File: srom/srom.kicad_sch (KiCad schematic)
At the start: 18 parts, among them J1 Conn_01x03_Female, Q1 PMBT2222A, U1 4075, U4 74LS245, U5 Pico-1 ROM

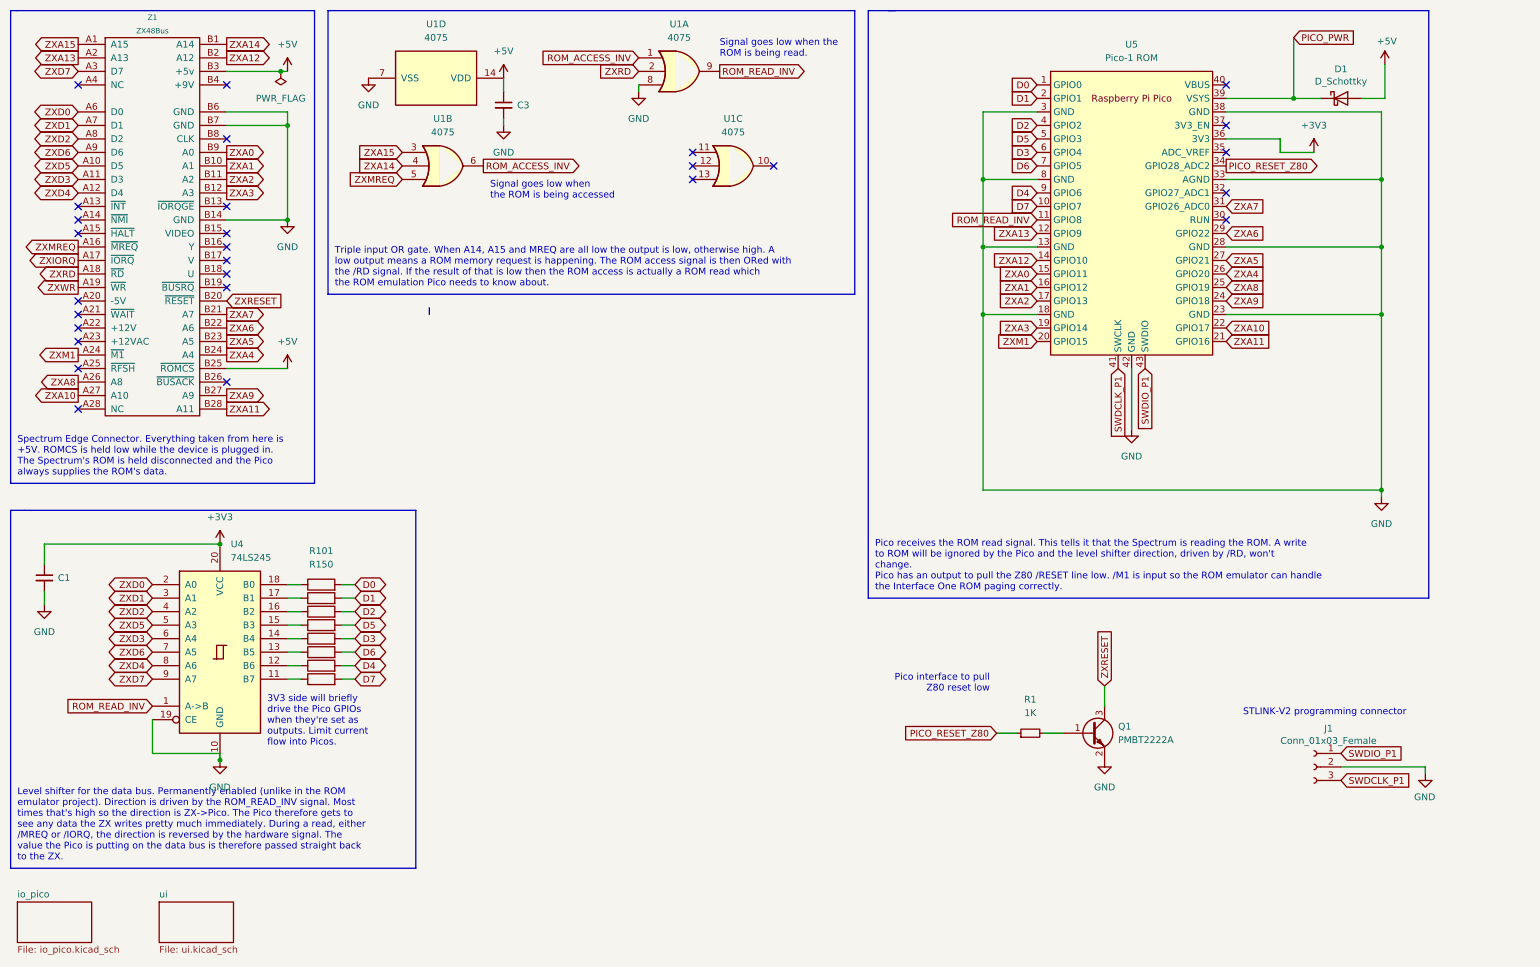
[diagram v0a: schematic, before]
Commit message: break out the 3V3 supplies into separate ones
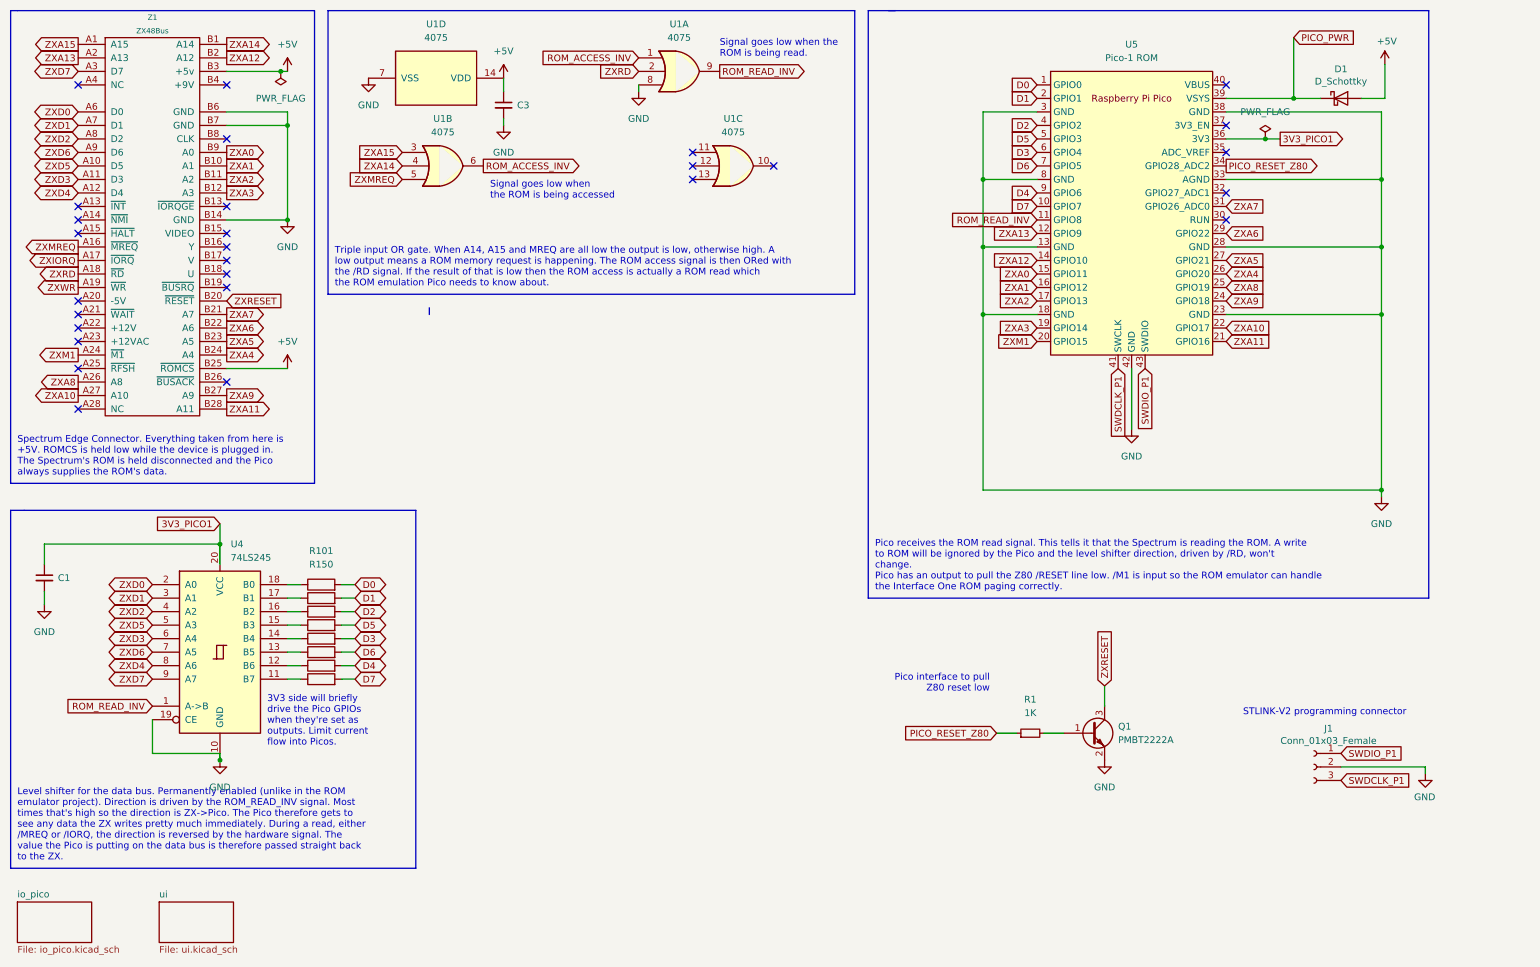
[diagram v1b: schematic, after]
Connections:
- net +3V3 renamed 3V3_PICO1
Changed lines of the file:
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@@
     (title "Pico Interface One")
     (date "2023-03-01")
-    (rev "v1.1")
+    (rev "v1.1 to v1.2 WIP")
+  )
+  (junction (at 196.85 72.39) (diameter 0) (color 0 0 0 0)
+  )
+  (junction (at 249.936 39.37) (diameter 0) (color 0 0 0 0)
   )
   (junction (at 53.34 115.57) (diameter 0) (color 0 0 0 0)
-  )
-  (junction (at 196.85 72.39) (diameter 0) (color 0 0 0 0)
   )
   (junction (at 196.85 59.69) (diameter 0) (color 0 0 0 0)
@@
     (stroke (width 0) (type default) (color 0 0 0 0))
   )
+  (wire (pts (xy 249.936 39.37) (xy 252.73 39.37))
+    (stroke (width 0) (type default) (color 0 0 0 0))
+  )
   (wire (pts (xy 54.61 26.67) (xy 64.77 26.67))
     (stroke (width 0) (type default) (color 0 0 0 0))
@@
     (stroke (width 0) (type default) (color 0 0 0 0))
   )
-  (wire (pts (xy 252.73 39.37) (xy 252.73 41.91))
-    (stroke (width 0) (type default) (color 0 0 0 0))
-  )
   (polyline (pts (xy 71.12 15.24) (xy 71.12 104.14))
     (stroke (width 0) (type default) (color 0 0 0 0))
@@
     (stroke (width 0) (type default) (color 0 0 0 0))
   )
+  (wire (pts (xy 53.34 115.57) (xy 53.34 119.38))
+    (stroke (width 0) (type default) (color 0 0 0 0))
+  )
   (wire (pts (xy 196.85 46.99) (xy 207.01 46.99))
     (stroke (width 0) (type default) (color 0 0 0 0))
@@
     (stroke (width 0) (type default) (color 0 0 0 0))
   )
-  (wire (pts (xy 252.73 41.91) (xy 259.08 41.91))
-    (stroke (width 0) (type default) (color 0 0 0 0))
-  )
   (wire (pts (xy 106.68 27.94) (xy 106.68 30.48))
     (stroke (width 0) (type default) (color 0 0 0 0))
@@
     (stroke (width 0) (type default) (color 0 0 0 0))
   )
+  (wire (pts (xy 53.34 111.76) (xy 53.34 115.57))
+    (stroke (width 0) (type default) (color 0 0 0 0))
+  )
   (wire (pts (xy 207.01 34.29) (xy 196.85 34.29))
     (stroke (width 0) (type default) (color 0 0 0 0))
@@
     (stroke (width 0) (type default) (color 0 0 0 0))
   )
-  (wire (pts (xy 242.57 39.37) (xy 252.73 39.37))
+  (wire (pts (xy 242.57 39.37) (xy 249.936 39.37))
     (stroke (width 0) (type default) (color 0 0 0 0))
   )
@@
     )
   )
+  (global_label "3V3_PICO1" (shape output) (at 252.73 39.37 0) (fields_autoplaced)
+    (effects (font (size 1.27 1.27)) (justify left))
+    (property "Intersheet References" "${INTERSHEET_REFS}" (id 0) (at 265.3031 39.2906 0)
+      (effects (font (size 1.27 1.27)) (justify left) hide)
+    )
+  )
   (global_label "D6" (shape input) (at 207.01 44.45 180) (fields_autoplaced)
     (effects (font (size 1.27 1.27)) (justify right))
@@
     )
   )
+  (global_label "3V3_PICO1" (shape input) (at 53.34 111.76 180) (fields_autoplaced)
+    (effects (font (size 1.27 1.27)) (justify right))
+    (property "Intersheet References" "${INTERSHEET_REFS}" (id 0) (at 40.7669 111.6806 0)
+      (effects (font (size 1.27 1.27)) (justify right) hide)
+    )
+  )
   (global_label "ZXA0" (shape input) (at 207.01 64.77 180) (fields_autoplaced)
     (effects (font (size 1.27 1.27)) (justify right))
@@
       (effects (font (size 1.27 1.27)) (justify right) hide)
     )
+  )
+  (symbol (lib_id "power:PWR_FLAG") (at 249.936 39.37 0) (unit 1)
+    (in_bom yes) (on_board yes) (fields_autoplaced)
+    (property "Reference" "#FLG0102" (id 0) (at 249.936 37.465 0)
+      (effects (font (size 1.27 1.27)) hide)
+    )
+    (property "Value" "PWR_FLAG" (id 1) (at 249.936 34.29 0))
+    (property "Footprint" "" (id 2) (at 249.936 39.37 0)
+      (effects (font (size 1.27 1.27)) hide)
+    )
+    (property "Datasheet" "~" (id 3) (at 249.936 39.37 0)
+      (effects (font (size 1.27 1.27)) hide)
+    )
+    (pin "1")
   )
   (symbol (lib_id "power:+5V") (at 272.415 25.4 0) (unit 1)
@@
     (pin "1")
     (pin "2")
-  )
-  (symbol (lib_id "power:+3V3") (at 259.08 41.91 0) (unit 1)
-    (in_bom yes) (on_board yes)
-    (property "Reference" "#PWR0101" (id 0) (at 259.08 45.72 0)
-      (effects (font (size 1.27 1.27)) hide)
-    )
-    (property "Value" "+3V3" (id 1) (at 259.08 36.83 0))
-    (property "Footprint" "" (id 2) (at 259.08 41.91 0)
-      (effects (font (size 1.27 1.27)) hide)
-    )
-    (property "Datasheet" "" (id 3) (at 259.08 41.91 0)
-      (effects (font (size 1.27 1.27)) hide)
-    )
-    (pin "1")
-  )
-  (symbol (lib_id "power:+3V3") (at 53.34 115.57 0) (unit 1)
-    (in_bom yes) (on_board yes) (fields_autoplaced)
-    (property "Reference" "#PWR010" (id 0) (at 53.34 119.38 0)
-      (effects (font (size 1.27 1.27)) hide)
-    )
-    (property "Value" "+3V3" (id 1) (at 53.34 110.49 0))
-    (property "Footprint" "" (id 2) (at 53.34 115.57 0)
-      (effects (font (size 1.27 1.27)) hide)
-    )
-    (property "Datasheet" "" (id 3) (at 53.34 115.57 0)
-      (effects (font (size 1.27 1.27)) hide)
-    )
-    (pin "1")
   )
   (symbol (lib_id "Device:R") (at 72.39 130.81 90) (unit 1)
@@
       (reference "#FLG0101") (unit 1) (value "PWR_FLAG") (footprint "")
     )
+    (path "/00435cad-35db-4d8c-a211-1a67f7361e91"
+      (reference "#FLG0102") (unit 1) (value "PWR_FLAG") (footprint "")
+    )
+    (path "/95a6eb69-d4c1-4a7e-a8e8-144430faf0e2/25fce74c-db7d-439d-b46a-e7ee4fba7d1a"
+      (reference "#FLG0103") (unit 1) (value "PWR_FLAG") (footprint "")
+    )
+    (path "/acda4c69-0a65-473b-ab4f-e765252d7da2/47f1e06f-c0f4-47be-b2ea-94c67d89ef70"
+      (reference "#FLG0104") (unit 1) (value "PWR_FLAG") (footprint "")
+    )
     (path "/acda4c69-0a65-473b-ab4f-e765252d7da2/334e052e-8ff6-4bbe-a873-da87ff53ae91"
       (reference "#FLG0301") (unit 1) (value "PWR_FLAG") (footprint "")
@@
       (reference "#PWR05") (unit 1) (value "+5V") (footprint "")
     )
-    (path "/680d1fc8-3a19-4cac-a3b2-5242d9ba4ad5"
-      (reference "#PWR010") (unit 1) (value "+3V3") (footprint "")
-    )
     (path "/e65b2d50-1512-4b2c-8e99-2f26673148c8"
       (reference "#PWR011") (unit 1) (value "GND") (footprint "")
@@
       (reference "#PWR016") (unit 1) (value "GND") (footprint "")
     )
-    (path "/64ca279f-08b9-4ba5-8585-3fc2b834e6f0"
-      (reference "#PWR0101") (unit 1) (value "+3V3") (footprint "")
-    )
     (path "/5344e888-6e86-4b4d-8c03-ed4967b31a8a"
       (reference "#PWR0102") (unit 1) (value "GND") (footprint "")
@@
       (reference "#PWR0201") (unit 1) (value "GND") (footprint "")
     )
-    (path "/95a6eb69-d4c1-4a7e-a8e8-144430faf0e2/c54c1e8a-e59e-4902-8ed1-8aca0d40aa2d"
-      (reference "#PWR0202") (unit 1) (value "+3V3") (footprint "")
-    )
     (path "/95a6eb69-d4c1-4a7e-a8e8-144430faf0e2/b4561307-559f-491e-95d1-1c57e89e9bd0"
       (reference "#PWR0203") (unit 1) (value "GND") (footprint "")
@@
       (reference "#PWR0204") (unit 1) (value "GND") (footprint "")
     )
-    (path "/95a6eb69-d4c1-4a7e-a8e8-144430faf0e2/31ee41c8-2e5c-4998-bf70-c3af77f7450a"
-      (reference "#PWR0205") (unit 1) (value "+3V3") (footprint "")
-    )
-    (path "/95a6eb69-d4c1-4a7e-a8e8-144430faf0e2/da16d1c0-e0fb-438f-b16b-b7064b2070b2"
-      (reference "#PWR0206") (unit 1) (value "+3V3") (footprint "")
-    )
     (path "/95a6eb69-d4c1-4a7e-a8e8-144430faf0e2/74d2792e-dc2e-4c26-bfe0-64794fa1d06e"
       (reference "#PWR0207") (unit 1) (value "GND") (footprint "")
@@
       (reference "#PWR0301") (unit 1) (value "GND") (footprint "")
     )
-    (path "/acda4c69-0a65-473b-ab4f-e765252d7da2/2f004ed8-568a-4db0-ae25-4b856d05e91a"
-      (reference "#PWR0302") (unit 1) (value "+3V3") (footprint "")
-    )
     (path "/acda4c69-0a65-473b-ab4f-e765252d7da2/9111f657-cc15-4eeb-9b4d-78f61ca6b08c"
       (reference "#PWR0303") (unit 1) (value "GND") (footprint "")
@@
       (reference "#PWR0304") (unit 1) (value "GND") (footprint "")
     )
-    (path "/acda4c69-0a65-473b-ab4f-e765252d7da2/0b79a16b-da0b-469f-b1f2-b6265ed1490c"
-      (reference "#PWR0305") (unit 1) (value "+3V3") (footprint "")
-    )
-    (path "/acda4c69-0a65-473b-ab4f-e765252d7da2/9fa9b51b-82ff-40db-902e-69e5796d2d81"
-      (reference "#PWR0306") (unit 1) (value "+3V3") (footprint "")
-    )
     (path "/acda4c69-0a65-473b-ab4f-e765252d7da2/a58c7f3b-6519-4b5a-8453-2d4882e5998e"
       (reference "#PWR0307") (unit 1) (value "GND") (footprint "")
@@
       (reference "#PWR0308") (unit 1) (value "GND") (footprint "")
     )
-    (path "/acda4c69-0a65-473b-ab4f-e765252d7da2/cc711933-4bb6-49a0-86db-e15cbb42ea8c"
-      (reference "#PWR0309") (unit 1) (value "+3V3") (footprint "")
-    )
     (path "/acda4c69-0a65-473b-ab4f-e765252d7da2/4d7c68d1-96f4-4474-b8ea-43bf3e5da187"
